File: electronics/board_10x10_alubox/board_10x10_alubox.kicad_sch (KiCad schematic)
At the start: 54 parts, among them J1 Proto, J10 module_2x15_right_input, J11 module_2x15_right_input, J12 module_2x15_right_input, J13 Conn_01x03, J14 Conn_01x03, J15 Conn_01x03, J16 Conn_01x03, J17 Conn_01x03, J18 Conn_01x03, J19 Conn_01x03, J2 Proto, J20 Conn_01x03, J21 Conn_01x03, J22 Conn_01x03, J23 Conn_01x03, J24 Conn_01x03, J3 Proto, J4 Proto, J5 module_2x15_left_output, J6 module_2x15_left_input, J7 module_2x15_left_input, J8 module_2x15_left_input, J9 module_2x15_right_output, SW1 switch_DPDT, SW2 switch_DPDT, SW3 switch_DPDT, SW4 switch_DPDT

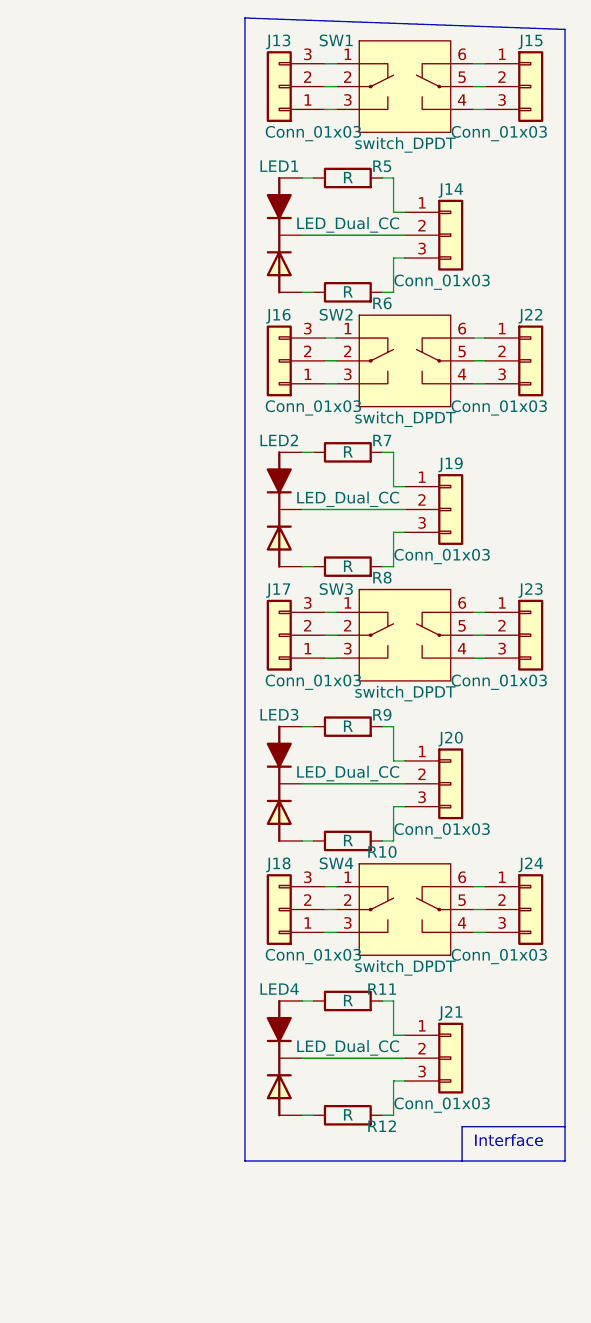
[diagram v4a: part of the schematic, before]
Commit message: fixed error with power switch pinout
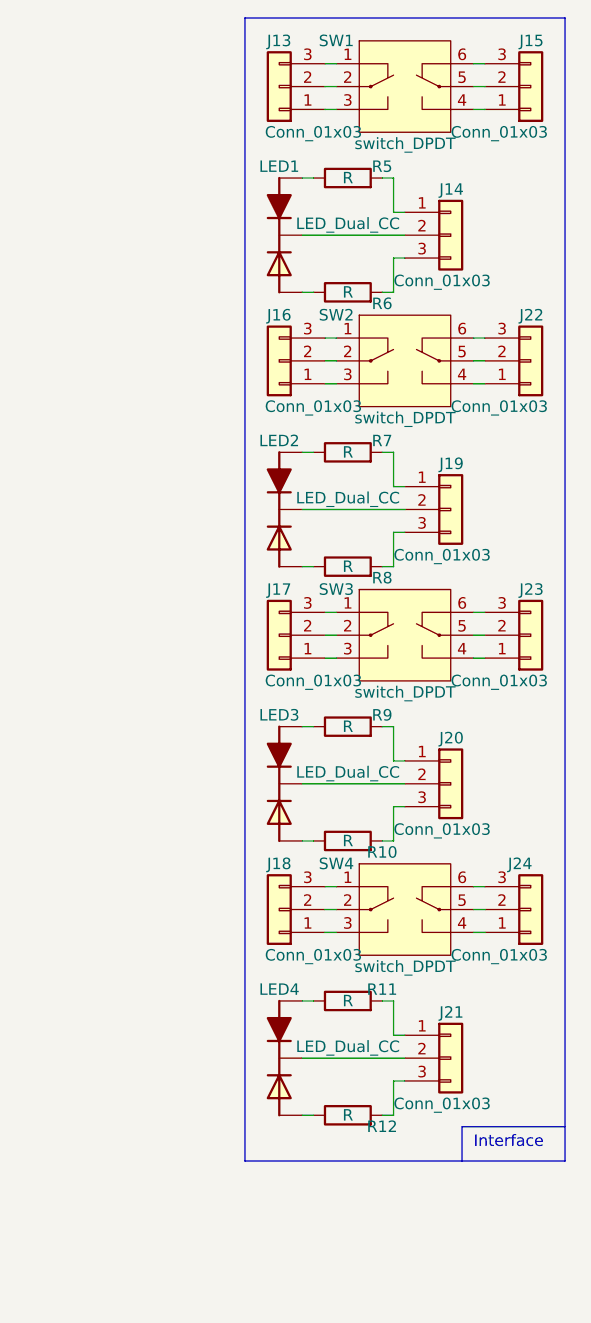
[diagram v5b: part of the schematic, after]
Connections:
- net at SW1.4 (SW2_P2): now also J15.1 (Pin_1); no longer J15.3 (Pin_3)
- net at SW1.6 (SW2_P2): now also J15.3 (Pin_3); no longer J15.1 (Pin_1)
- net at J24.1 (Pin_1): now also SW4.4 (SW2_P2); no longer SW4.6 (SW2_P2)
- net at J24.3 (Pin_3): now also SW4.6 (SW2_P2); no longer SW4.4 (SW2_P2)
- net at SW2.4 (SW2_P2): now also J22.1 (Pin_1); no longer J22.3 (Pin_3)
- net at SW2.6 (SW2_P2): now also J22.3 (Pin_3); no longer J22.1 (Pin_1)
- net at SW3.4 (SW2_P2): now also J23.1 (Pin_1); no longer J23.3 (Pin_3)
- net at SW3.6 (SW2_P2): now also J23.3 (Pin_3); no longer J23.1 (Pin_1)
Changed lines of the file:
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@@
     (stroke (width 0) (type default) (color 0 0 0 0))
   )
-  (polyline (pts (xy 280.67 16.51) (xy 245.11 15.24))
+  (polyline (pts (xy 280.67 15.24) (xy 245.11 15.24))
     (stroke (width 0) (type default) (color 0 0 0 0))
   )
@@
     (stroke (width 0) (type default) (color 0 0 0 0))
   )
-  (polyline (pts (xy 280.67 142.24) (xy 280.67 16.51))
+  (polyline (pts (xy 280.67 142.24) (xy 280.67 15.24))
     (stroke (width 0) (type default) (color 0 0 0 0))
   )
@@
     (pin "1")
   )
-  (symbol (lib_id "Connector_Generic:Conn_01x03") (at 276.86 114.3 0) (unit 1)
+  (symbol (lib_id "Connector_Generic:Conn_01x03") (at 276.86 114.3 0) (mirror x) (unit 1)
     (in_bom yes) (on_board yes)
-    (property "Reference" "J24" (id 0) (at 275.59 109.22 0)
+    (property "Reference" "J24" (id 0) (at 274.32 109.22 0)
       (effects (font (size 1.27 1.27)) (justify left))
     )
@@
     (pin "2")
   )
-  (symbol (lib_id "Connector_Generic:Conn_01x03") (at 276.86 22.86 0) (unit 1)
+  (symbol (lib_id "Connector_Generic:Conn_01x03") (at 276.86 22.86 0) (mirror x) (unit 1)
     (in_bom yes) (on_board yes)
     (property "Reference" "J15" (id 0) (at 275.59 17.78 0)
@@
     (pin "1")
   )
-  (symbol (lib_id "Connector_Generic:Conn_01x03") (at 276.86 83.82 0) (unit 1)
+  (symbol (lib_id "Connector_Generic:Conn_01x03") (at 276.86 83.82 0) (mirror x) (unit 1)
     (in_bom yes) (on_board yes)
     (property "Reference" "J23" (id 0) (at 275.59 78.74 0)
@@
     (pin "1")
   )
-  (symbol (lib_id "Connector_Generic:Conn_01x03") (at 276.86 53.34 0) (unit 1)
+  (symbol (lib_id "Connector_Generic:Conn_01x03") (at 276.86 53.34 0) (mirror x) (unit 1)
     (in_bom yes) (on_board yes)
     (property "Reference" "J22" (id 0) (at 275.59 48.26 0)

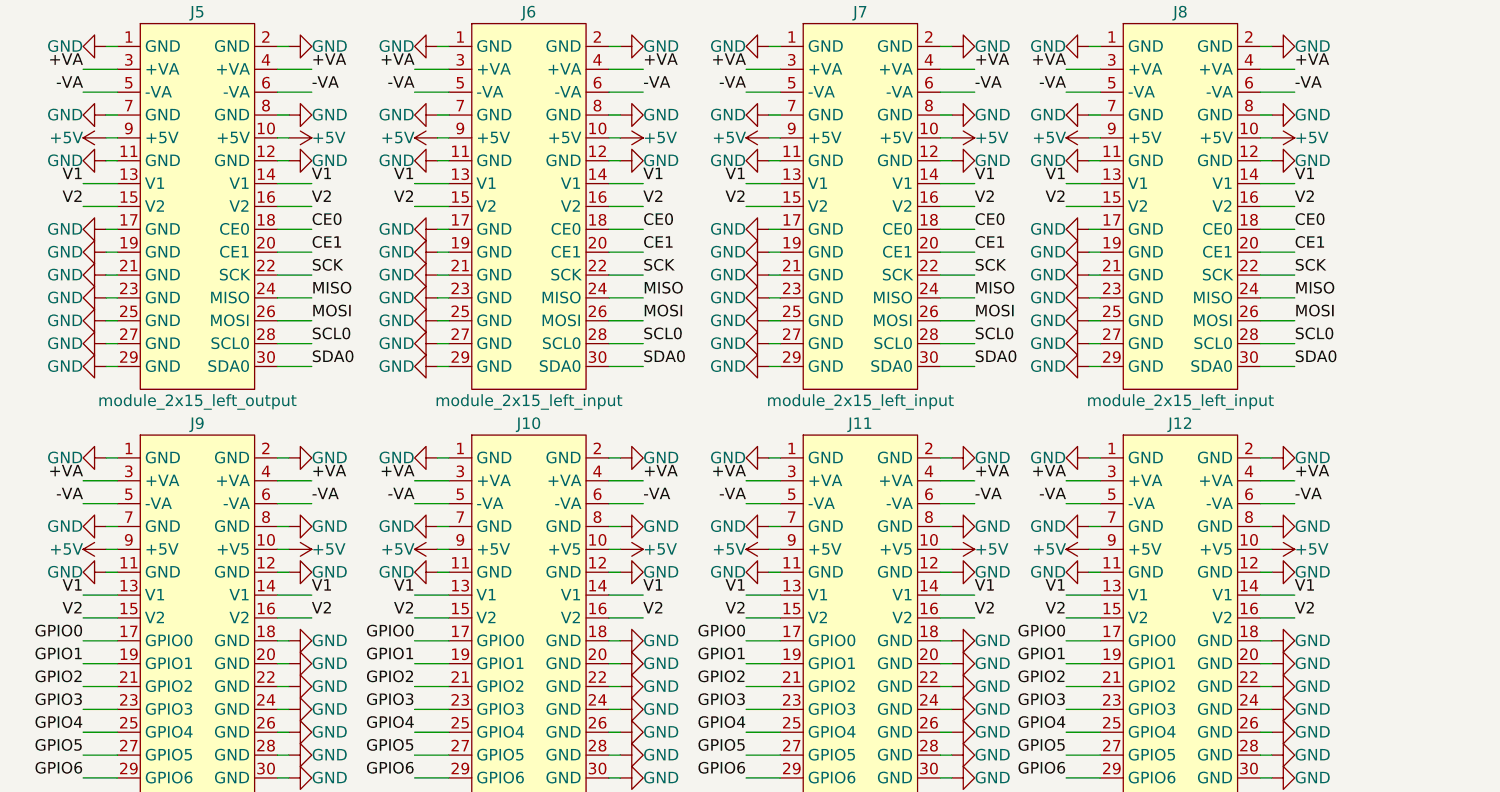
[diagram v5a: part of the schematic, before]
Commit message: updated pinouts
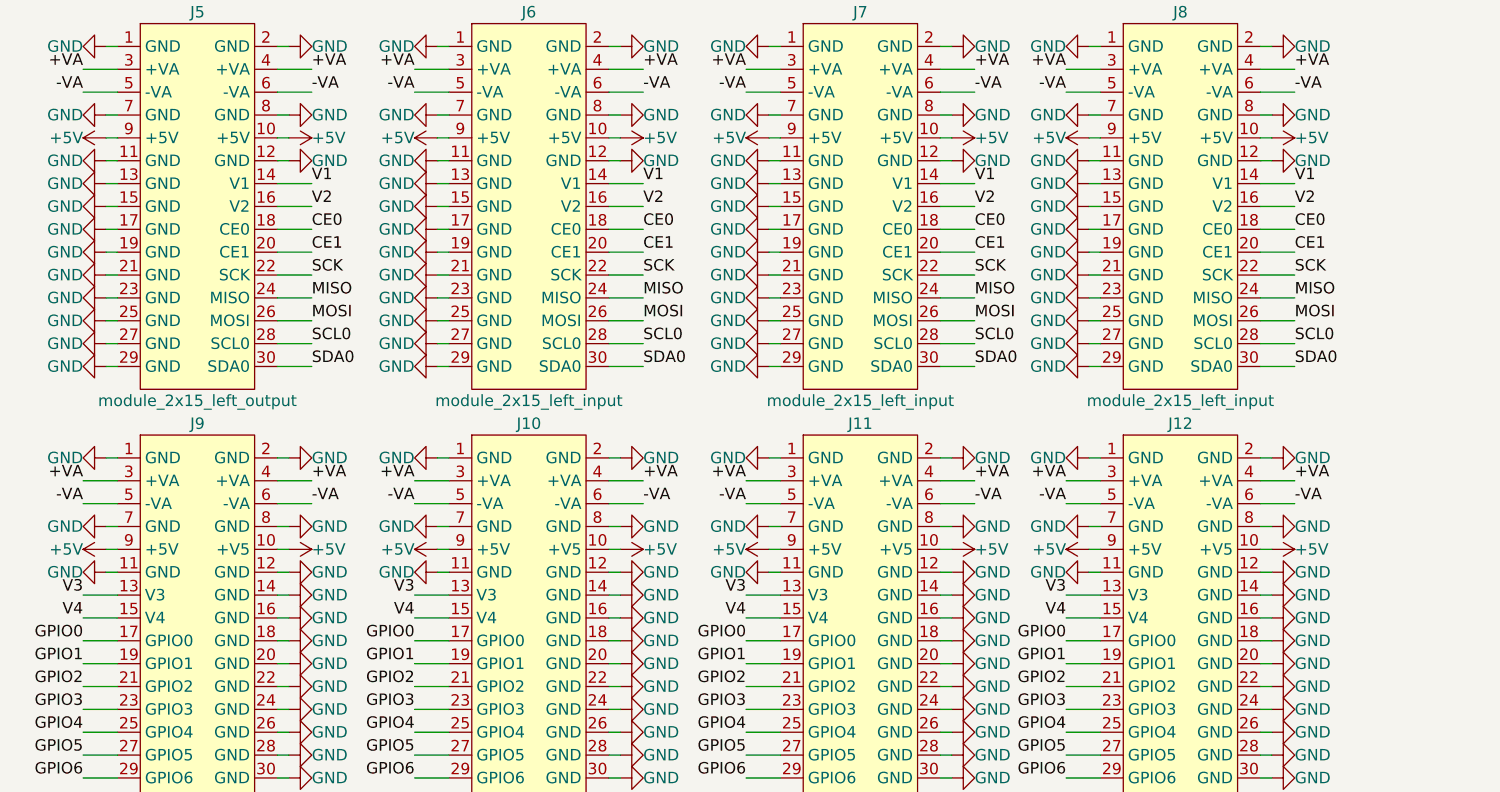
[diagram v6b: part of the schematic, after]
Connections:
- net GND: now also J10.14 (GND), J10.16 (GND), J11.14 (GND), J11.16 (GND), J12.14 (GND), J12.16 (GND), J5.13 (GND), J5.15 (GND), J6.13 (GND), J6.15 (GND), J7.13 (GND), J7.15 (GND), J8.13 (GND), J8.15 (GND), J9.14 (GND), J9.16 (GND)
- net V1: no longer J10.13 (V1), J10.14 (V1), J11.13 (V1), J11.14 (V1), J12.13 (V1), J12.14 (V1), J5.13 (V1), J6.13 (V1), J7.13 (V1), J8.13 (V1), J9.13 (V1), J9.14 (V1)
- net V2: no longer J10.15 (V2), J10.16 (V2), J11.15 (V2), J11.16 (V2), J12.15 (V2), J12.16 (V2), J5.15 (V2), J6.15 (V2), J7.15 (V2), J8.15 (V2), J9.15 (V2), J9.16 (V2)
- new net V3: J10.13 (V3), J11.13 (V3), J12.13 (V3), J9.13 (V3)
- new net V4: J10.15 (V4), J11.15 (V4), J12.15 (V4), J9.15 (V4)

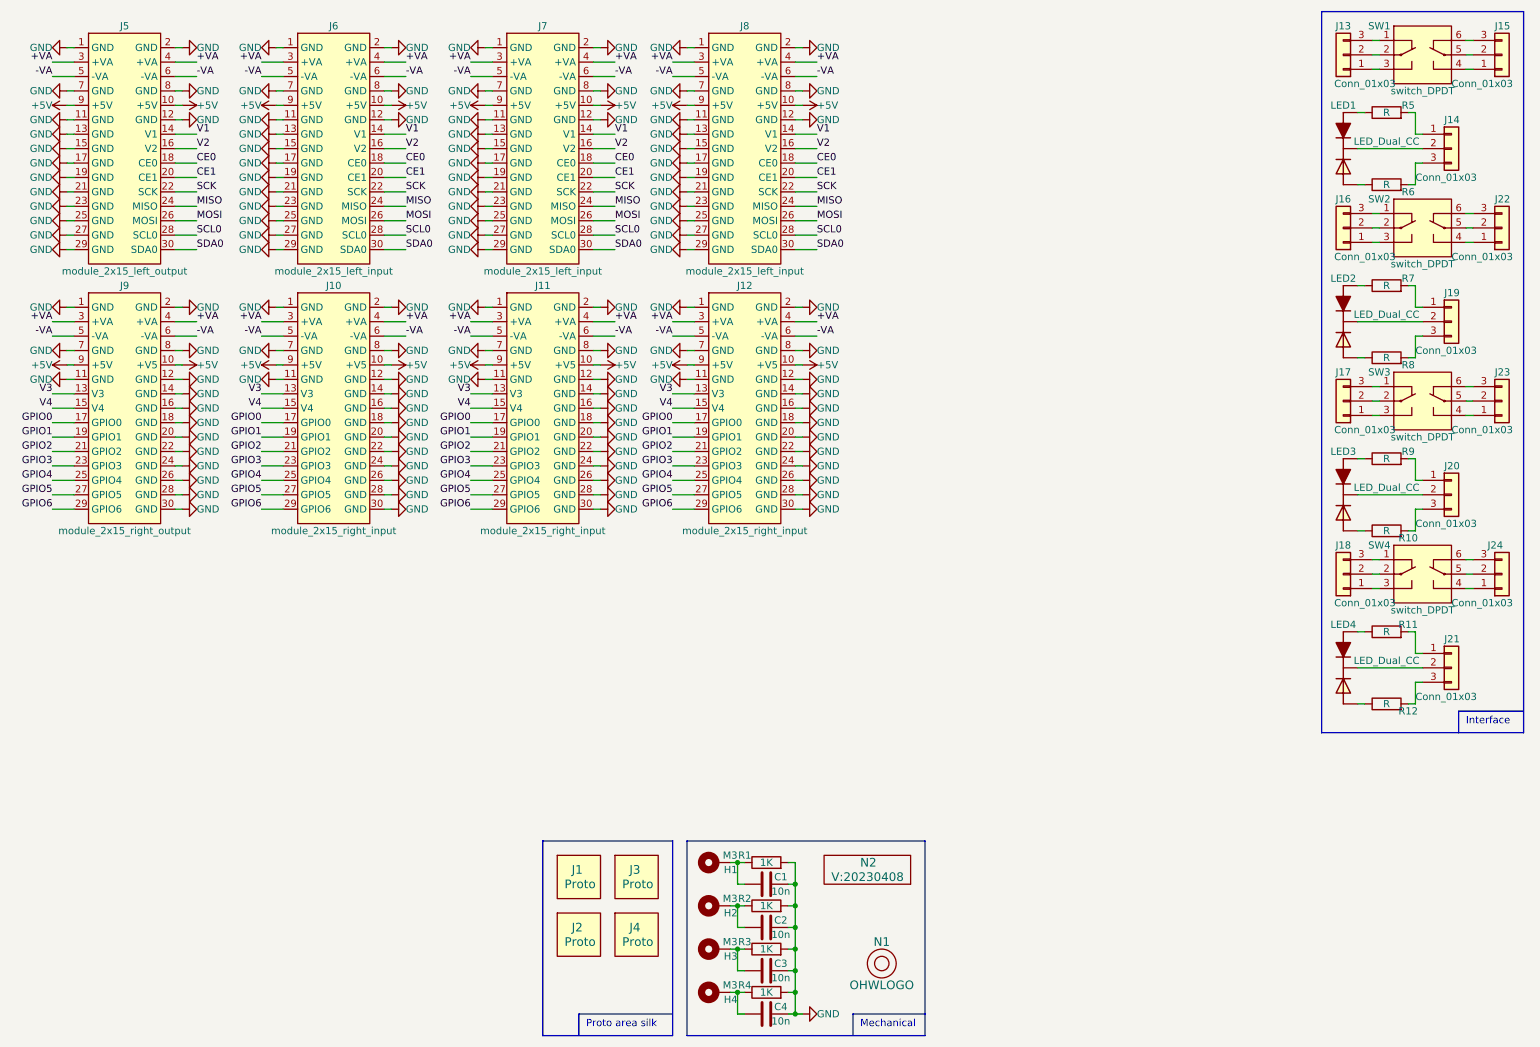
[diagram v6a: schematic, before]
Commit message: routed new voltage rails
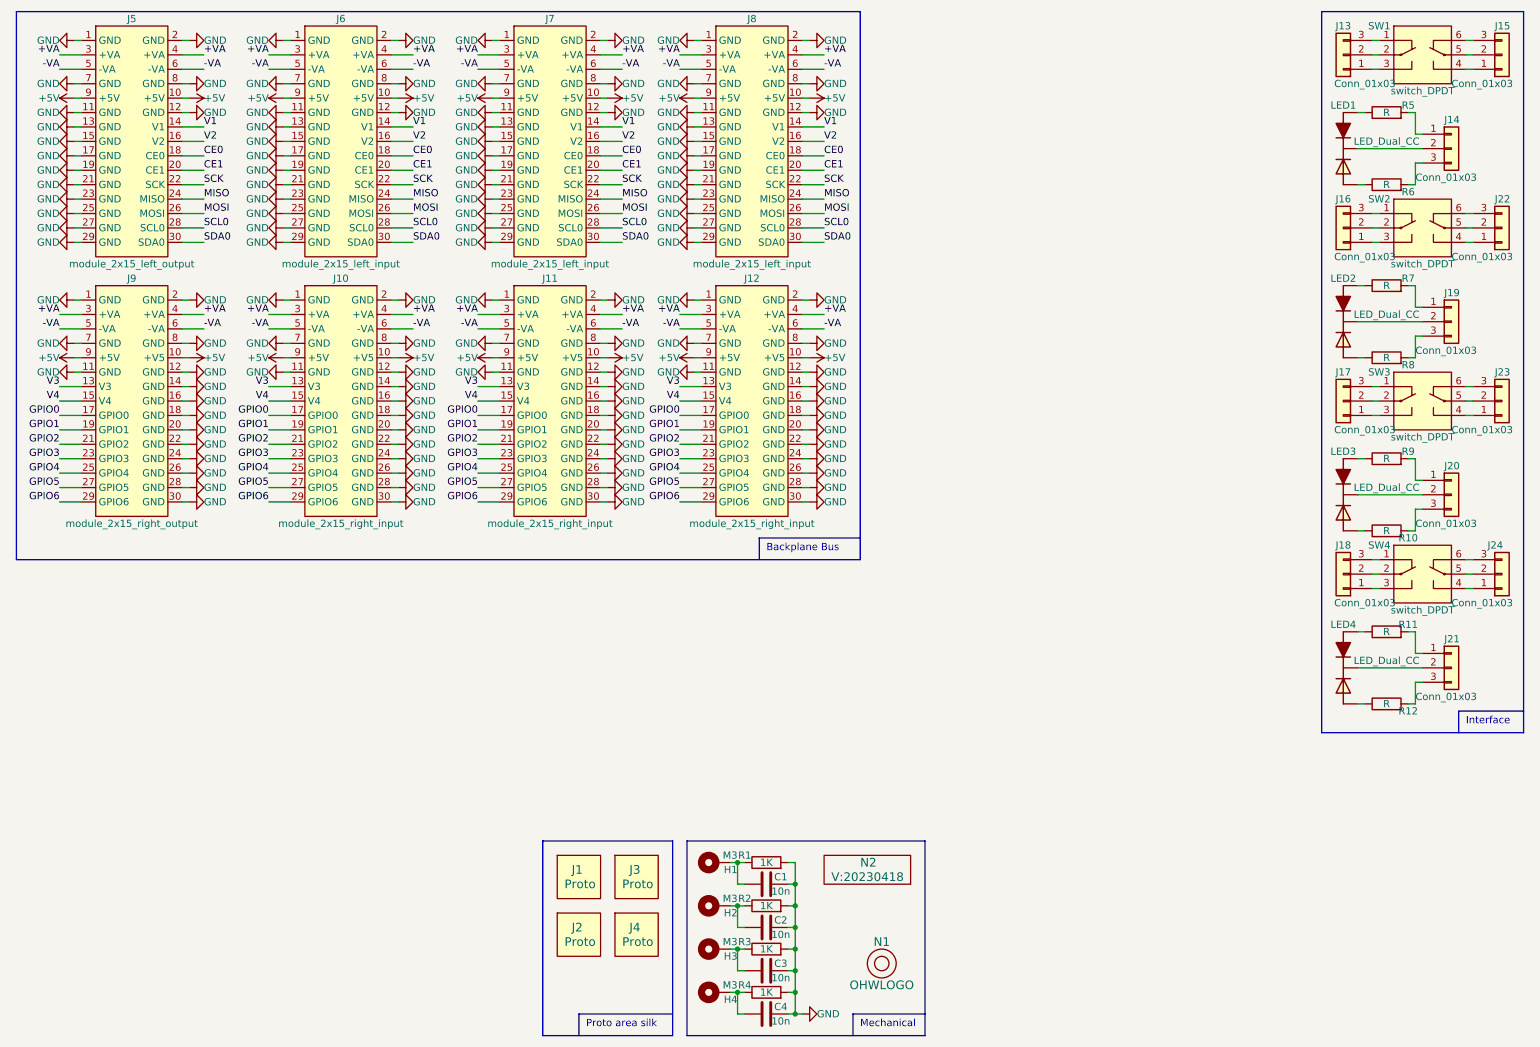
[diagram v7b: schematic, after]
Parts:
- N2: value V:20230408 -> V:20230418
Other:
- note added: "Backplane Bus"
- moved on the sheet: J10, J11, J12, J5, J6, J7, J8, J9

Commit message: updated versionnumber
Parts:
- N2: value V:20230418 -> V:20230501
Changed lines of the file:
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@@
       (effects (font (size 1.524 1.524)) (justify left))
     )
-    (property "Value" "V:20230418" (id 1) (at 158.75 167.64 0)
+    (property "Value" "V:20230501" (id 1) (at 158.75 167.64 0)
       (effects (font (size 1.524 1.524)) (justify left))
     )
@@
     )
     (path "/00000000-0000-0000-0000-00005da0a665"
-      (reference "N2") (unit 1) (value "V:20230418") (footprint "SquantorLabels:Label_Generic")
+      (reference "N2") (unit 1) (value "V:20230501") (footprint "SquantorLabels:Label_Generic")
     )
     (path "/dec54ea0-0c0f-4872-abfa-f0c07a94c65b"
